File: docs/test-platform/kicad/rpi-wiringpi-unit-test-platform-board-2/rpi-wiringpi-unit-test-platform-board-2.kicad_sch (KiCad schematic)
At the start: 18 parts, among them J1 IN_PWR_SERVO, J2 IN_I2C_SPI, J3 IN_CS_SR, J4 Servo, M1 ADS1115_0x48, SW1 SW_DIP_x02, U1 74HC595, U2 MCP3008, U3 MCP4922, U4 MCP42010

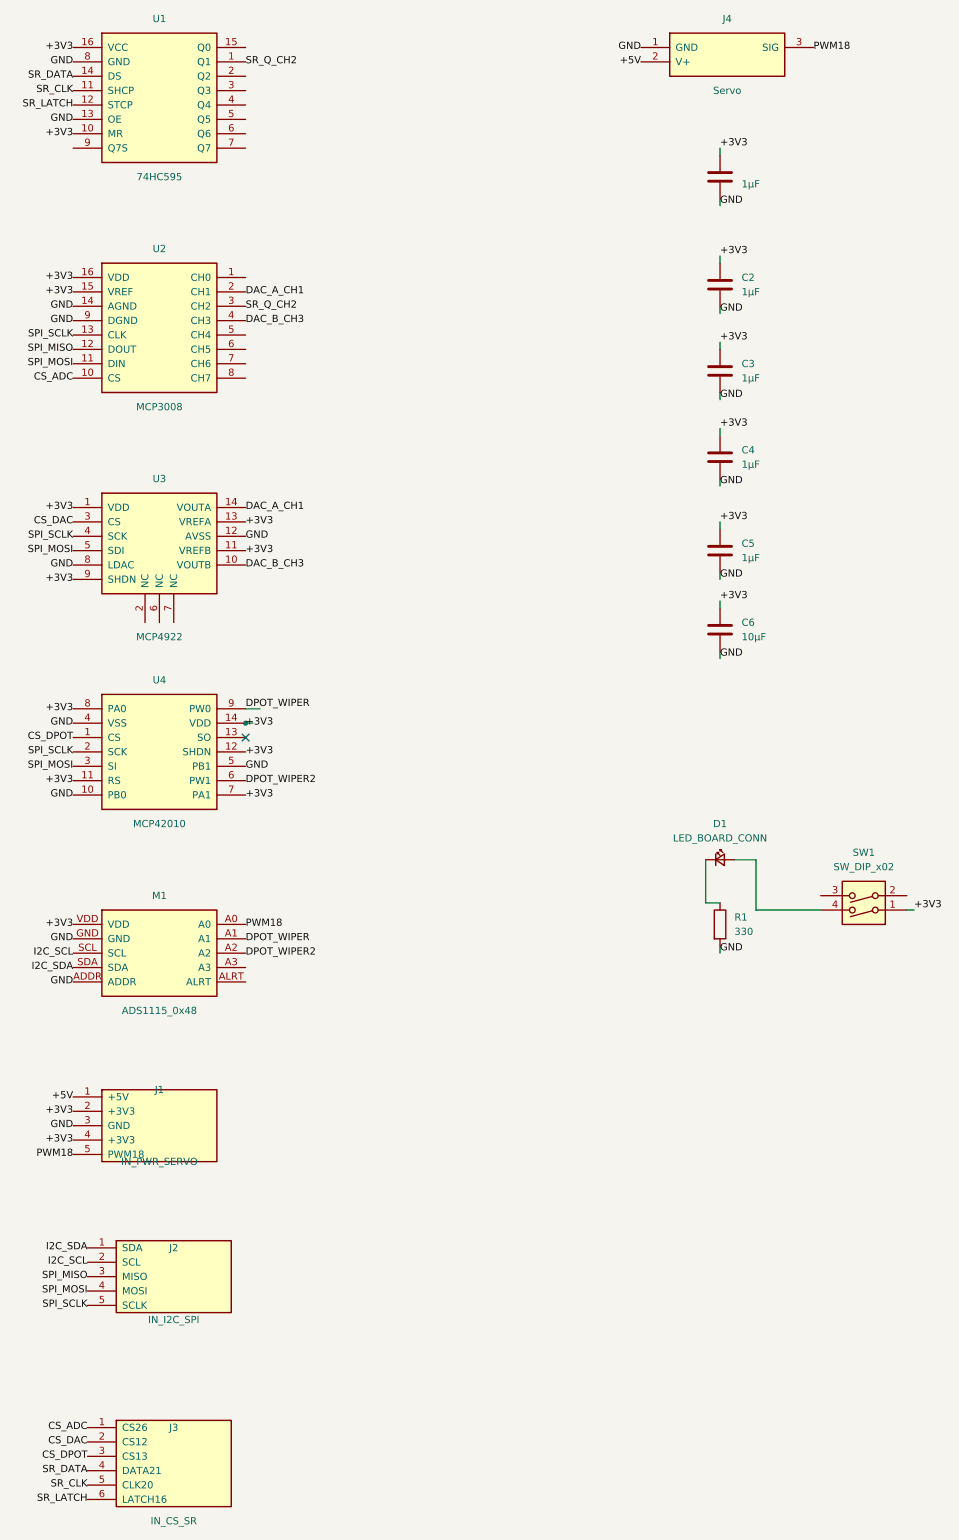
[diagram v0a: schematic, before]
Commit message: Added N/C to unconnected pins; Swapped out double pole switch for single
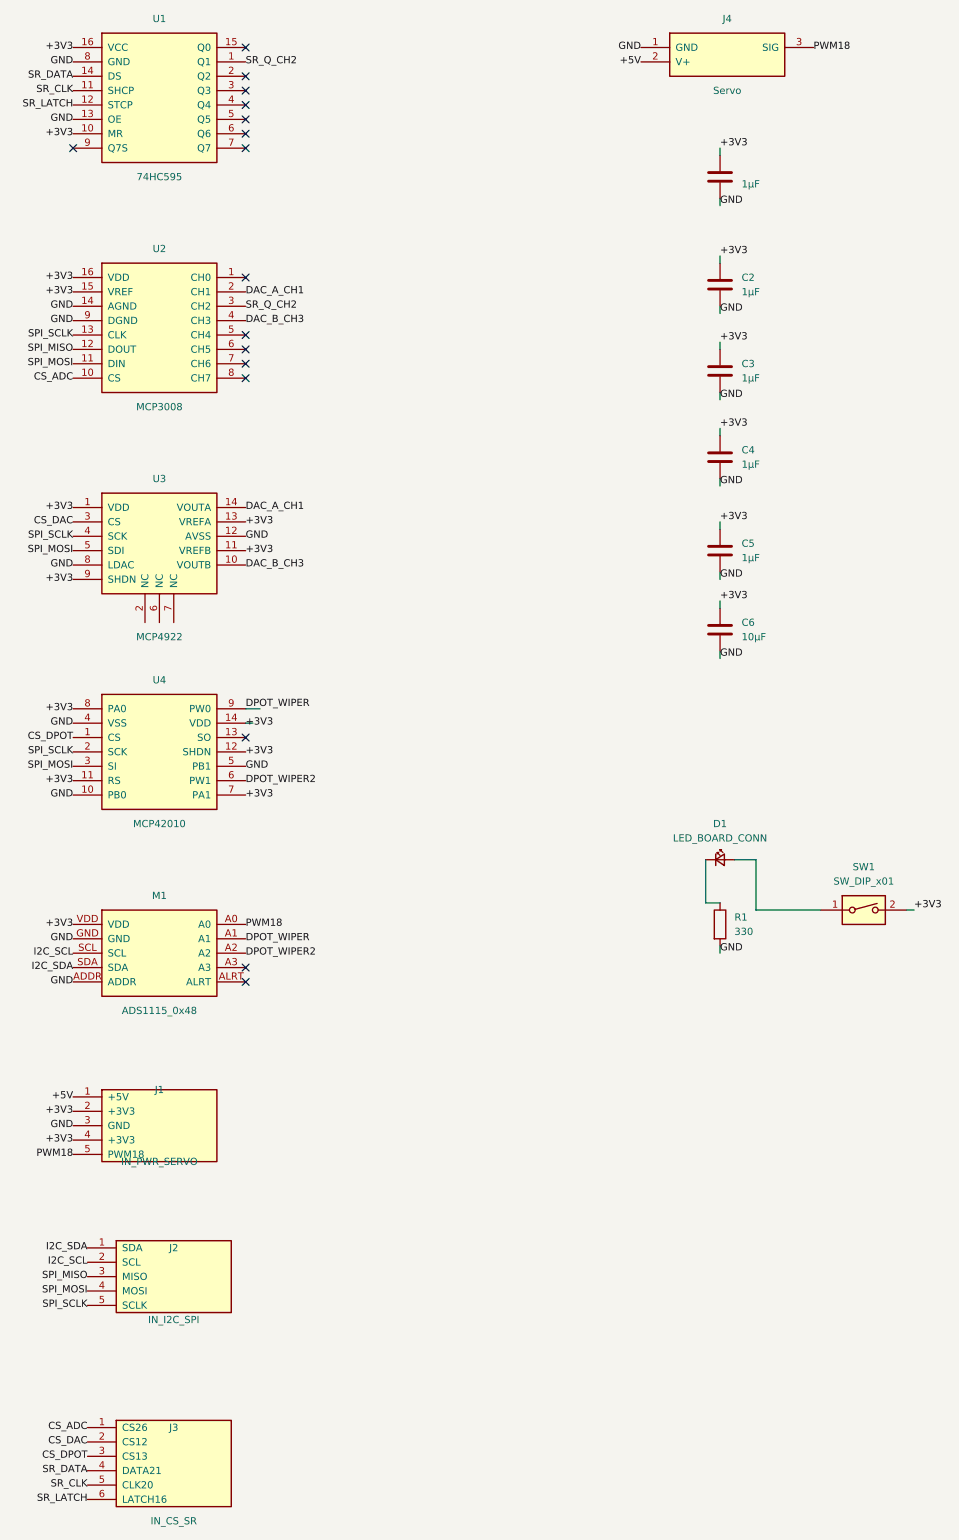
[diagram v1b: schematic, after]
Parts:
- removed SW1: SW_DIP_x02, Button_Switch_THT:SW_DIP_SPSTx02_Slide_9.78x7.26mm_W7.62mm_P2.54mm, symbol Switch:SW_DIP_x02
- added SW1: SW_DIP_x01, Button_Switch_THT:SW_DIP_SPSTx01_Slide_9.78x4.72mm_W7.62mm_P2.54mm, symbol Switch:SW_DIP_x01
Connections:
- net +3V3: now also SW1.2
- net at D1.2 (A): now also SW1.1
- no-connect marks 1 -> 16
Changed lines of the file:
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@@
 	(generator_version "10.0")
 	(paper "User" 240 372.24)
-	(junction
-		(at 85.09 147.32)
-		(diameter 0)
-		(color 0 0 0 0)
+	(no_connect
+		(at 85.09 190.5)
+	)
+	(no_connect
+		(at 85.09 43.18)
+	)
+	(no_connect
+		(at 85.09 83.82)
+	)
+	(no_connect
+		(at 85.09 78.74)
 	)
 	(no_connect
 		(at 85.09 149.86)
+	)
+	(no_connect
+		(at 85.09 35.56)
+	)
+	(no_connect
+		(at 85.09 38.1)
+	)
+	(no_connect
+		(at 85.09 33.02)
+	)
+	(no_connect
+		(at 85.09 27.94)
+	)
+	(no_connect
+		(at 85.09 68.58)
+	)
+	(no_connect
+		(at 85.09 86.36)
+	)
+	(no_connect
+		(at 85.09 40.64)
+	)
+	(no_connect
+		(at 54.61 45.72)
+	)
+	(no_connect
+		(at 85.09 45.72)
+	)
+	(no_connect
+		(at 85.09 193.04)
+	)
+	(no_connect
+		(at 85.09 81.28)
 	)
 	(wire
@@
 	)
 	(symbol
+		(lib_id "Switch:SW_DIP_x01")
+		(at 194.31 180.34 0)
+		(unit 1)
+		(body_style 1)
+		(exclude_from_sim no)
+		(in_bom yes)
+		(on_board yes)
+		(in_pos_files yes)
+		(dnp no)
+		(fields_autoplaced yes)
+		(property "Reference" "SW1"
+			(at 194.31 172.72 0)
+			(show_name no)
+			(do_not_autoplace no)
+			(effects
+				(font
+					(size 1.27 1.27)
+				)
+			)
+		)
+		(property "Value" "SW_DIP_x01"
+			(at 194.31 175.26 0)
+			(show_name no)
+			(do_not_autoplace no)
+			(effects
+				(font
+					(size 1.27 1.27)
+				)
+			)
+		)
+		(property "Footprint" "Button_Switch_THT:SW_DIP_SPSTx01_Slide_9.78x4.72mm_W7.62mm_P2.54mm"
+			(at 194.31 180.34 0)
+			(hide yes)
+			(show_name no)
+			(do_not_autoplace no)
+			(effects
+				(font
+					(size 1.27 1.27)
+				)
+			)
+		)
+		(property "Datasheet" ""
+			(at 194.31 180.34 0)
+			(hide yes)
+			(show_name no)
+			(do_not_autoplace no)
+			(effects
+				(font
+					(size 1.27 1.27)
+				)
+			)
+		)
+		(property "Description" "1x DIP Switch, Single Pole Single Throw (SPST) switch, small symbol"
+			(at 194.31 180.34 0)
+			(hide yes)
+			(show_name no)
+			(do_not_autoplace no)
+			(effects
+				(font
+					(size 1.27 1.27)
+				)
+			)
+		)
+		(pin "1"
+		)
+		(pin "2"
+		)
+		(instances
+			(project "rpi-wiringpi-unit-test-platform-board-2"
+				(path "/7946ceed-5e50-51f0-9396-19e4533fa9f5"
+					(reference "SW1")
+					(unit 1)
+				)
+			)
+		)
+	)
+	(symbol
 		(lib_id "Device:LED_Small")
 		(at 168.91 171.45 0)
@@
 					(unit 1)
 				)
-			)
-		)
-	)
-	(symbol
-		(lib_id "Switch:SW_DIP_x02")
-		(at 194.31 177.8 180)
-		(unit 1)
-		(body_style 1)
-		(exclude_from_sim no)
-		(in_bom yes)
-		(on_board yes)
-		(in_pos_files yes)
-		(dnp no)
-		(fields_autoplaced yes)
-		(property "Reference" "SW1"
-			(at 194.31 170.18 0)
-			(show_name no)
-			(do_not_autoplace no)
-			(effects
-				(font
-					(size 1.27 1.27)
-				)
-			)
-		)
-		(property "Value" "SW_DIP_x02"
-			(at 194.31 172.72 0)
-			(show_name no)
-			(do_not_autoplace no)
-			(effects
-				(font
-					(size 1.27 1.27)
-				)
-			)
-		)
-		(property "Footprint" "Button_Switch_THT:SW_DIP_SPSTx02_Slide_9.78x7.26mm_W7.62mm_P2.54mm"
-			(at 194.31 177.8 0)
-			(hide yes)
-			(show_name no)
-			(do_not_autoplace no)
-			(effects
-				(font
-					(size 1.27 1.27)
-				)
-			)
-		)
-		(property "Datasheet" ""
-			(at 194.31 177.8 0)
-			(hide yes)
-			(show_name no)
-			(do_not_autoplace no)
-			(effects
-				(font
-					(size 1.27 1.27)
-				)
-			)
-		)
-		(property "Description" "2x DIP Switch, Single Pole Single Throw (SPST) switch, small symbol"
-			(at 194.31 177.8 0)
-			(hide yes)
-			(show_name no)
-			(do_not_autoplace no)
-			(effects
-				(font
-					(size 1.27 1.27)
-				)
-			)
-		)
-		(pin "2"
-		)
-		(pin "1"
-		)
-		(pin "3"
-		)
-		(pin "4"
-		)
-		(instances
-			(project "rpi-wiringpi-unit-test-platform-board-2"
-				(path "/7946ceed-5e50-51f0-9396-19e4533fa9f5"
-					(reference "SW1")
-					(unit 1)
-				)
